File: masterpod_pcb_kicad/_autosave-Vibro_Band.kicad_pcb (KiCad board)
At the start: 2 copper layers, 9 parts, among them U1 ULN2003A, U2 MPU-6050, U3 XIAO-ESP32-C3-SMD

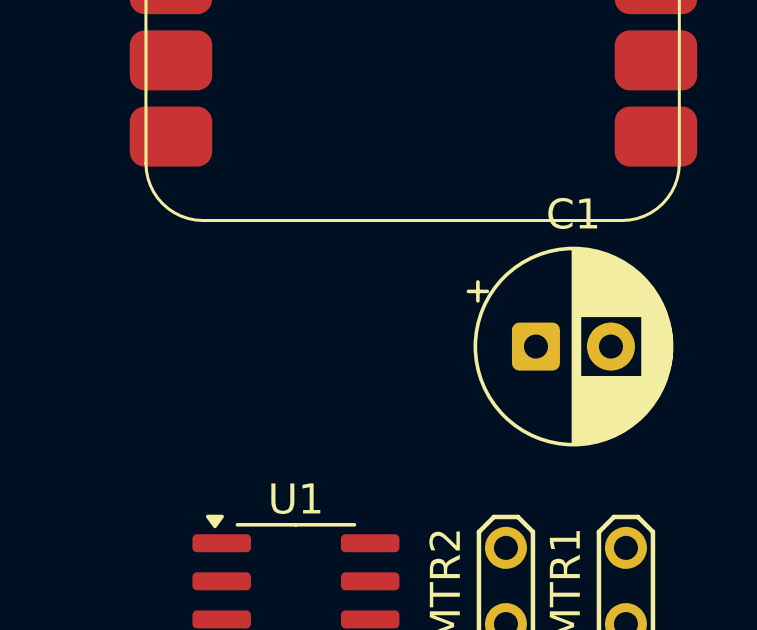
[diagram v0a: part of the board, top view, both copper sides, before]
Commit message: band working to test motor with new ULN2003a Driver
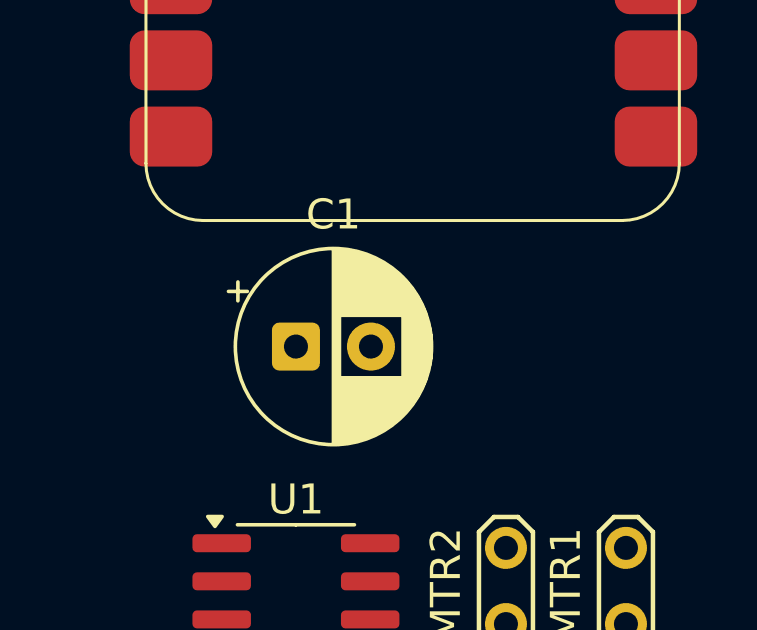
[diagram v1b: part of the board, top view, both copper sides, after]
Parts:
- moved C1 8.00 mm to (105.0, 77.0)
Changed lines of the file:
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@@
 	(footprint "Capacitor_THT:CP_Radial_D6.3mm_P2.50mm"
 		(layer "F.Cu")
-		(at 113 77)
+		(at 105 77)
 		(descr "CP, Radial series, Radial, pin pitch=2.50mm, diameter=6.3mm, height=7mm, Electrolytic Capacitor")
 		(tags "CP Radial series Radial pin pitch 2.50mm diameter 6.3mm height 7mm Electrolytic Capacitor")
